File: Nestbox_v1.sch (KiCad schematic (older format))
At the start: 27 parts, among them P1 RX/TX, P2 TST/RST, P3 VDD/GND, Q1 SFH 3605, SW1 SMD-BUTTON_2P-3.0X2.5X1.2+0.4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, U1 MSP430FR5969, Y1 Crystal

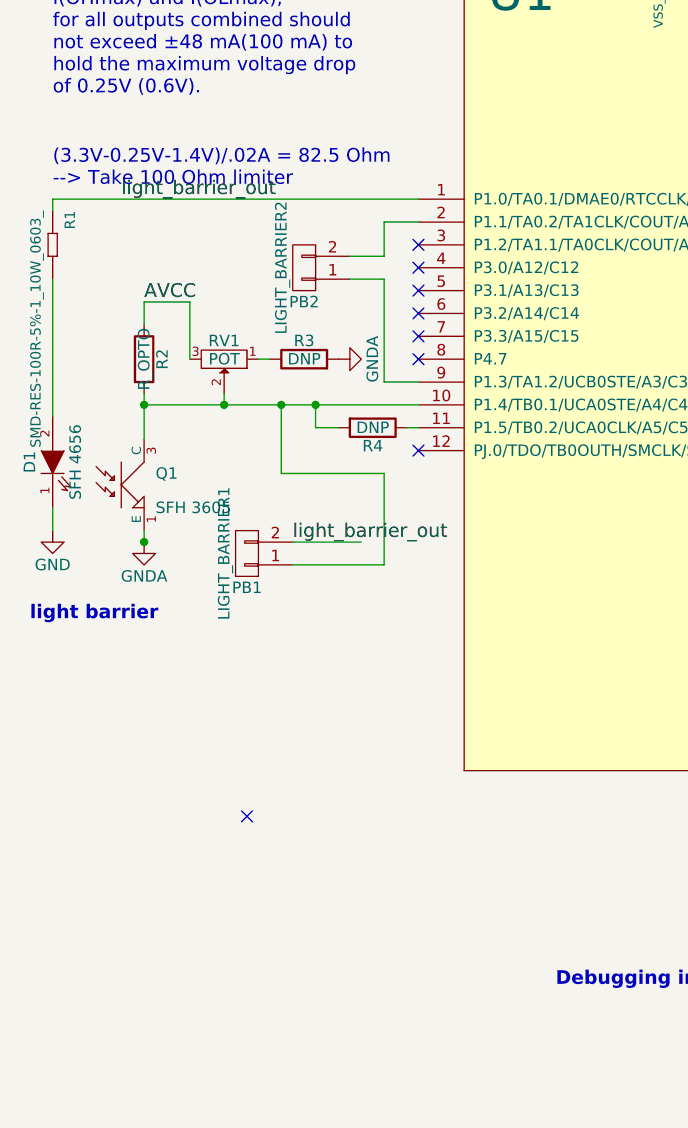
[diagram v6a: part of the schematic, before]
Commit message: added second phototransistor. started routing power and analog traces
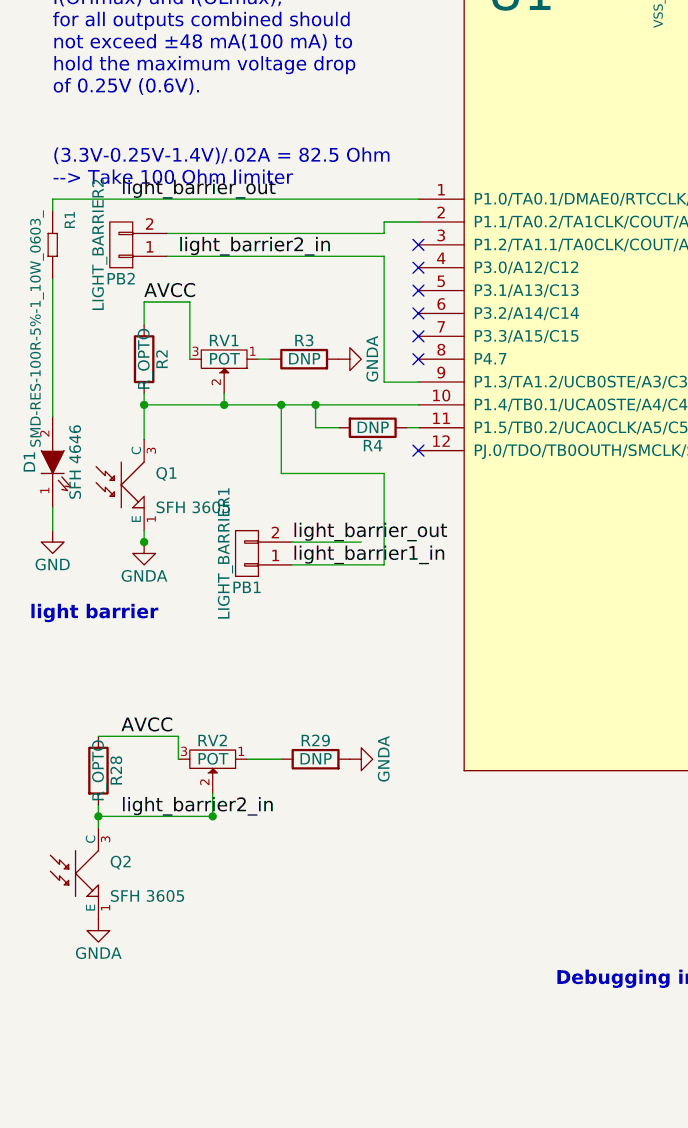
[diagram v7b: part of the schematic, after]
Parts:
- added Q2: SFH 3605, Octanis3:MIDLED_phototransistor, symbol OPTO_NPN
- added R28: R_OPTO, Resistors_SMD:R_0603, symbol R
- added R29: DNP, Resistors_SMD:R_0603, symbol R
- added RV2: POT, pot:3223G, symbol POT-RESCUE-Nestbox_v1
- D1: value SFH 4656 -> SFH 4646
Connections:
- net AVCC: now also R28.1, RV2.3
- net GND: now also Q2.1 (E), R29.2
- net light_barrier1_in: now reaches PB1.1 (P1), Q1.3 (C), R2.2, R4.2, RV1.2, U1.10 (P1.4/TB0.1/UCA0STE/A4/C4)
- net light_barrier2_in: now reaches PB2.1 (P1), U1.9 (P1.3/TA1.2/UCB0STE/A3/C3)
- net light_barrier2_in: now also Q2.3 (C), R28.2, RV2.2
- new net: R29.1, RV2.1
- no-connect marks 20 -> 19
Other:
- moved on the sheet: PB2
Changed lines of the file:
@@
 P 650 4250
 F 0 "D1" H 650 4350 50  0000 C CNN
-F 1 "SFH 4656" H 650 4150 50  0000 C CNN
+F 1 "SFH 4646" H 650 4150 50  0000 C CNN
 F 2 "Octanis3:MIDLED" H 650 4250 50  0001 C CNN
 F 3 "" H 650 4250 50  0000 C CNN
@@
 Wire Wire Line
 	3150 1750 3150 1800
-NoConn ~ 1500 5800
 $Comp
 L CERAMIC-10UF-25V-10%-X5R_0805_ C4
@@
 L CONN_01X02 PB2
 U 1 1 58BA717E
-P 1750 3400
-F 0 "PB2" H 1750 3550 50  0000 C CNN
-F 1 "LIGHT_BARRIER2" V 1850 3400 50  0000 C CNN
-F 2 "Socket_Strips:Socket_Strip_Straight_1x02" H 1750 3400 50  0001 C CNN
-F 3 "" H 1750 3400 50  0000 C CNN
-	1    1750 3400
+P 950 3300
+F 0 "PB2" H 950 3450 50  0000 C CNN
+F 1 "LIGHT_BARRIER2" V 1050 3300 50  0000 C CNN
+F 2 "Socket_Strips:Socket_Strip_Straight_1x02" H 950 3300 50  0001 C CNN
+F 3 "" H 950 3300 50  0000 C CNN
+	1    950  3300
 	-1   0    0    1
 $EndComp
@@
 	2250 3900 2100 3900
 Wire Wire Line
-	2100 3900 2100 3450
-Wire Wire Line
-	2100 3450 1950 3450
+	2100 3900 2100 3350
+Wire Wire Line
+	2100 3350 1150 3350
 Wire Wire Line
 	2250 3200 2100 3200
 Wire Wire Line
-	2100 3200 2100 3350
-Wire Wire Line
-	2100 3350 1950 3350
+	2100 3200 2100 3250
+Wire Wire Line
+	2100 3250 1150 3250
 Wire Wire Line
 	4800 6000 5600 6000
@@
 Text Label 1700 4600 0    60   ~ 0
 light_barrier_out
+$Comp
+L GNDA #PWR032
+U 1 1 58BD1039
+P 850 6250
+F 0 "#PWR032" H 850 6000 50  0001 C CNN
+F 1 "GNDA" H 850 6100 50  0000 C CNN
+F 2 "" H 850 6250 50  0000 C CNN
+F 3 "" H 850 6250 50  0000 C CNN
+	1    850  6250
+	1    0    0    -1
+$EndComp
+$Comp
+L OPTO_NPN Q2
+U 1 1 58BD10E6
+P 750 6050
+F 0 "Q2" H 900 6100 50  0000 L CNN
+F 1 "SFH 3605" H 900 5950 50  0000 L CNN
+F 2 "Octanis3:MIDLED_phototransistor" H 750 6050 50  0001 C CNN
+F 3 "" H 750 6050 50  0000 C CNN
+	1    750  6050
+	1    0    0    -1
+$EndComp
+$Comp
+L R R28
+U 1 1 58BD118C
+P 850 5600
+F 0 "R28" V 930 5600 50  0000 C CNN
+F 1 "R_OPTO" V 850 5600 50  0000 C CNN
+F 2 "Resistors_SMD:R_0603" V 780 5600 50  0001 C CNN
+F 3 "" H 850 5600 50  0000 C CNN
+	1    850  5600
+	1    0    0    -1
+$EndComp
+$Comp
+L POT-RESCUE-Nestbox_v1 RV2
+U 1 1 58BD120A
+P 1350 5550
+F 0 "RV2" H 1350 5470 50  0000 C CNN
+F 1 "POT" H 1350 5550 50  0000 C CNN
+F 2 "pot:3223G" H 1350 5550 50  0001 C CNN
+F 3 "" H 1350 5550 50  0000 C CNN
+	1    1350 5550
+	-1   0    0    1
+$EndComp
+$Comp
+L R R29
+U 1 1 58BD1294
+P 1800 5550
+F 0 "R29" V 1880 5550 50  0000 C CNN
+F 1 "DNP" V 1800 5550 50  0000 C CNN
+F 2 "Resistors_SMD:R_0603" V 1730 5550 50  0001 C CNN
+F 3 "" H 1800 5550 50  0000 C CNN
+	1    1800 5550
+	0    -1   -1   0
+$EndComp
+Wire Wire Line
+	850  5450 1200 5450
+Wire Wire Line
+	1200 5450 1200 5550
+Wire Wire Line
+	1500 5550 1650 5550
+$Comp
+L GNDA #PWR033
+U 1 1 58BD155D
+P 1950 5550
+F 0 "#PWR033" H 1950 5300 50  0001 C CNN
+F 1 "GNDA" H 1950 5400 50  0000 C CNN
+F 2 "" H 1950 5550 50  0000 C CNN
+F 3 "" H 1950 5550 50  0000 C CNN
+	1    1950 5550
+	0    -1   -1   0
+$EndComp
+Text Label 950  5450 0    60   ~ 0
+AVCC
+Text Label 1700 4700 0    60   ~ 0
+light_barrier1_in
+Text Label 950  5800 0    60   ~ 0
+light_barrier2_in
+Text Label 1200 3350 0    60   ~ 0
+light_barrier2_in
+Wire Wire Line
+	1350 5800 1350 5700
+Wire Wire Line
+	850  5750 850  5850
+Wire Wire Line
+	850  5800 1350 5800
+Connection ~ 1350 5800
+Connection ~ 850  5800
 $EndSCHEMATC

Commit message: added schematic changes
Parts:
- added C29: CERAMIC-100NF-50V-10%-X7R_0603_, SeeedOPL-Capacitor-2016:C0603, symbol CERAMIC-100NF-50V-10%-X7R_0603_
- added R30: SMD-RES-10K-1%-1_10W_0603_, SeeedOPL-Resistor-2016:R0603, symbol SMD-RES-10K-1%-1_10W_0603_
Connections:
- net GND: now also C29.2
- net at R7.1, SW1.2, U1.18 (P4.2/A10): now also R30.1
- new net: C29.1, R30.2
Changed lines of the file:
@@
 $EndComp
 $Comp
-L GND #PWR01
+L GND #PWR25
 U 1 1 586416A7
 P 6850 3100
-F 0 "#PWR01" H 6850 2850 50  0001 C CNN
+F 0 "#PWR25" H 6850 2850 50  0001 C CNN
 F 1 "GND" H 6850 2950 50  0000 C CNN
 F 2 "" H 6850 3100 50  0000 C CNN
@@
 $EndComp
 $Comp
-L +3.3V #PWR02
+L +3.3V #PWR17
 U 1 1 586418DC
 P 5000 1450
-F 0 "#PWR02" H 5000 1300 50  0001 C CNN
+F 0 "#PWR17" H 5000 1300 50  0001 C CNN
 F 1 "+3.3V" H 5000 1590 50  0000 C CNN
 F 2 "" H 5000 1450 50  0000 C CNN
@@
 $EndComp
 $Comp
-L GND #PWR03
+L GND #PWR7
 U 1 1 58641ADD
 P 3200 1600
-F 0 "#PWR03" H 3200 1350 50  0001 C CNN
+F 0 "#PWR7" H 3200 1350 50  0001 C CNN
 F 1 "GND" H 3200 1450 50  0000 C CNN
 F 2 "" H 3200 1600 50  0000 C CNN
@@
 $EndComp
 $Comp
-L +3.3V #PWR04
+L +3.3V #PWR8
 U 1 1 58641B00
 P 3550 1050
-F 0 "#PWR04" H 3550 900 50  0001 C CNN
+F 0 "#PWR8" H 3550 900 50  0001 C CNN
 F 1 "+3.3V" H 3550 1190 50  0000 C CNN
 F 2 "" H 3550 1050 50  0000 C CNN
@@
 $EndComp
 $Comp
-L GND #PWR05
+L GND #PWR18
 U 1 1 58652F3A
 P 5350 1800
-F 0 "#PWR05" H 5350 1550 50  0001 C CNN
+F 0 "#PWR18" H 5350 1550 50  0001 C CNN
 F 1 "GND" H 5350 1650 50  0000 C CNN
 F 2 "" H 5350 1800 50  0000 C CNN
@@
 $EndComp
 $Comp
-L GND #PWR06
+L GND #PWR11
 U 1 1 5865358A
 P 4100 950
-F 0 "#PWR06" H 4100 700 50  0001 C CNN
+F 0 "#PWR11" H 4100 700 50  0001 C CNN
 F 1 "GND" H 4100 800 50  0000 C CNN
 F 2 "" H 4100 950 50  0000 C CNN
@@
 $EndComp
 $Comp
-L GND #PWR07
+L GND #PWR27
 U 1 1 5865405F
 P 7500 1000
-F 0 "#PWR07" H 7500 750 50  0001 C CNN
+F 0 "#PWR27" H 7500 750 50  0001 C CNN
 F 1 "GND" H 7500 850 50  0000 C CNN
 F 2 "" H 7500 1000 50  0000 C CNN
@@
 $EndComp
 $Comp
-L +3.3V #PWR08
+L +3.3V #PWR29
 U 1 1 58654094
 P 7750 1000
-F 0 "#PWR08" H 7750 850 50  0001 C CNN
+F 0 "#PWR29" H 7750 850 50  0001 C CNN
 F 1 "+3.3V" H 7750 1140 50  0000 C CNN
 F 2 "" H 7750 1000 50  0000 C CNN
@@
 $EndComp
 $Comp
-L PWR_FLAG #FLG09
+L PWR_FLAG #FLG3
 U 1 1 58654135
 P 7750 1000
-F 0 "#FLG09" H 7750 1095 50  0001 C CNN
+F 0 "#FLG3" H 7750 1095 50  0001 C CNN
 F 1 "PWR_FLAG" H 7750 1180 50  0000 C CNN
 F 2 "" H 7750 1000 50  0000 C CNN
@@
 $EndComp
 $Comp
-L GND #PWR010
+L GND #PWR1
 U 1 1 587A72FE
 P 650 4550
-F 0 "#PWR010" H 650 4300 50  0001 C CNN
+F 0 "#PWR1" H 650 4300 50  0001 C CNN
 F 1 "GND" H 650 4400 50  0000 C CNN
 F 2 "" H 650 4550 50  0000 C CNN
@@
 $EndComp
 $Comp
-L GNDA #PWR011
+L GNDA #PWR4
 U 1 1 587B665F
 P 1900 3800
-F 0 "#PWR011" H 1900 3550 50  0001 C CNN
+F 0 "#PWR4" H 1900 3550 50  0001 C CNN
 F 1 "GNDA" H 1900 3650 50  0000 C CNN
 F 2 "" H 1900 3800 50  0000 C CNN
@@
 $EndComp
 $Comp
-L GNDA #PWR012
+L GNDA #PWR3
 U 1 1 587B6770
 P 1050 4600
-F 0 "#PWR012" H 1050 4350 50  0001 C CNN
+F 0 "#PWR3" H 1050 4350 50  0001 C CNN
 F 1 "GNDA" H 1050 4450 50  0000 C CNN
 F 2 "" H 1050 4600 50  0000 C CNN
@@
 $EndComp
 $Comp
-L GNDA #PWR013
+L GNDA #PWR9
 U 1 1 587B6902
 P 4000 1750
-F 0 "#PWR013" H 4000 1500 50  0001 C CNN
+F 0 "#PWR9" H 4000 1500 50  0001 C CNN
 F 1 "GNDA" H 4000 1600 50  0000 C CNN
 F 2 "" H 4000 1750 50  0000 C CNN
@@
 $EndComp
 $Comp
-L GNDA #PWR014
+L GNDA #PWR12
 U 1 1 587B69F1
 P 4300 1750
-F 0 "#PWR014" H 4300 1500 50  0001 C CNN
+F 0 "#PWR12" H 4300 1500 50  0001 C CNN
 F 1 "GNDA" H 4300 1600 50  0000 C CNN
 F 2 "" H 4300 1750 50  0000 C CNN
@@
 $EndComp
 $Comp
-L GNDA #PWR015
+L GNDA #PWR14
 U 1 1 587B6A2F
 P 4600 1750
-F 0 "#PWR015" H 4600 1500 50  0001 C CNN
+F 0 "#PWR14" H 4600 1500 50  0001 C CNN
 F 1 "GNDA" H 4600 1600 50  0000 C CNN
 F 2 "" H 4600 1750 50  0000 C CNN
@@
 $EndComp
 $Comp
-L GND #PWR016
+L GND #PWR15
 U 1 1 587B96DD
 P 4650 6400
-F 0 "#PWR016" H 4650 6150 50  0001 C CNN
+F 0 "#PWR15" H 4650 6150 50  0001 C CNN
 F 1 "GND" H 4650 6250 50  0000 C CNN
 F 2 "" H 4650 6400 50  0000 C CNN
@@
 $EndComp
 $Comp
-L +3.3V #PWR017
+L +3.3V #PWR16
 U 1 1 587B9736
 P 4650 7600
-F 0 "#PWR017" H 4650 7450 50  0001 C CNN
+F 0 "#PWR16" H 4650 7450 50  0001 C CNN
 F 1 "+3.3V" H 4650 7740 50  0000 C CNN
 F 2 "" H 4650 7600 50  0000 C CNN
@@
 $EndComp
 $Comp
-L GND #PWR018
+L GND #PWR13
 U 1 1 587B97E4
 P 4300 6850
-F 0 "#PWR018" H 4300 6600 50  0001 C CNN
+F 0 "#PWR13" H 4300 6600 50  0001 C CNN
 F 1 "GND" H 4300 6700 50  0000 C CNN
 F 2 "" H 4300 6850 50  0000 C CNN
@@
 $EndComp
 $Comp
-L GND #PWR019
+L GND #PWR10
 U 1 1 587B9834
 P 4000 6850
-F 0 "#PWR019" H 4000 6600 50  0001 C CNN
+F 0 "#PWR10" H 4000 6600 50  0001 C CNN
 F 1 "GND" H 4000 6700 50  0000 C CNN
 F 2 "" H 4000 6850 50  0000 C CNN
@@
 $EndComp
 $Comp
-L +3.3V #PWR020
+L +3.3V #PWR22
 U 1 1 587BBBBA
 P 6200 6300
-F 0 "#PWR020" H 6200 6150 50  0001 C CNN
+F 0 "#PWR22" H 6200 6150 50  0001 C CNN
 F 1 "+3.3V" H 6200 6440 50  0000 C CNN
 F 2 "" H 6200 6300 50  0000 C CNN
@@
 $EndComp
 $Comp
-L GND #PWR021
+L GND #PWR21
 U 1 1 587BBC10
 P 6100 6300
-F 0 "#PWR021" H 6100 6050 50  0001 C CNN
+F 0 "#PWR21" H 6100 6050 50  0001 C CNN
 F 1 "GND" H 6100 6150 50  0000 C CNN
 F 2 "" H 6100 6300 50  0000 C CNN
@@
 LORA_RX
 $Comp
-L +BATT #PWR022
+L +BATT #PWR30
 U 1 1 587BD5F5
 P 8000 1000
-F 0 "#PWR022" H 8000 850 50  0001 C CNN
+F 0 "#PWR30" H 8000 850 50  0001 C CNN
 F 1 "+BATT" H 8000 1140 50  0000 C CNN
 F 2 "" H 8000 1000 50  0000 C CNN
@@
 $EndComp
 $Comp
-L PWR_FLAG #FLG023
+L PWR_FLAG #FLG4
 U 1 1 587BD64F
 P 8000 1000
-F 0 "#FLG023" H 8000 1095 50  0001 C CNN
+F 0 "#FLG4" H 8000 1095 50  0001 C CNN
 F 1 "PWR_FLAG" H 8000 1180 50  0000 C CNN
 F 2 "" H 8000 1000 50  0000 C CNN
@@
 NoConn ~ 4900 1800
 $Comp
-L PWR_FLAG #FLG024
+L PWR_FLAG #FLG1
 U 1 1 587C02BB
 P 7500 900
-F 0 "#FLG024" H 7500 995 50  0001 C CNN
+F 0 "#FLG1" H 7500 995 50  0001 C CNN
 F 1 "PWR_FLAG" H 7500 1080 50  0000 C CNN
 F 2 "" H 7500 900 50  0000 C CNN
@@
 $EndComp
 $Comp
-L GND #PWR025
+L GND #PWR26
 U 1 1 587C0E96
 P 6950 1050
-F 0 "#PWR025" H 6950 800 50  0001 C CNN
+F 0 "#PWR26" H 6950 800 50  0001 C CNN
 F 1 "GND" H 6950 900 50  0000 C CNN
 F 2 "" H 6950 1050 50  0000 C CNN
@@
 $EndComp
 $Comp
-L GNDA #PWR026
+L GNDA #PWR24
 U 1 1 587C0F20
 P 6750 1050
-F 0 "#PWR026" H 6750 800 50  0001 C CNN
+F 0 "#PWR24" H 6750 800 50  0001 C CNN
 F 1 "GNDA" H 6750 900 50  0000 C CNN
 F 2 "" H 6750 1050 50  0000 C CNN
@@
 $EndComp
 $Comp
-L GNDPWR #PWR027
+L GNDPWR #PWR23
 U 1 1 587C0FCC
 P 6550 1100
-F 0 "#PWR027" H 6550 900 50  0001 C CNN
+F 0 "#PWR23" H 6550 900 50  0001 C CNN
 F 1 "GNDPWR" H 6550 970 50  0000 C CNN
 F 2 "" H 6550 1050 50  0000 C CNN
@@
 	4650 7100 4650 7200
 Wire Wire Line
-	4650 7150 4550 7150
+	4550 7150 4800 7150
 Wire Wire Line
 	4550 7150 4550 6100
@@
 	7300 4000 6850 4000
 $Comp
-L VDDA #PWR028
+L VDDA #PWR28
 U 1 1 587C8C74
 P 7500 1500
-F 0 "#PWR028" H 7500 1350 50  0001 C CNN
+F 0 "#PWR28" H 7500 1350 50  0001 C CNN
 F 1 "VDDA" H 7500 1650 50  0000 C CNN
 F 2 "" H 7500 1500 50  0000 C CNN
@@
 $EndComp
 $Comp
-L PWR_FLAG #FLG029
+L PWR_FLAG #FLG2
 U 1 1 587C8CD0
 P 7500 1500
-F 0 "#FLG029" H 7500 1595 50  0001 C CNN
+F 0 "#FLG2" H 7500 1595 50  0001 C CNN
 F 1 "PWR_FLAG" H 7500 1680 50  0000 C CNN
 F 2 "" H 7500 1500 50  0000 C CNN
@@
 	4000 6550 4000 6500
 $Comp
-L GND #PWR030
+L GND #PWR6
 U 1 1 587D2523
 P 3150 1800
-F 0 "#PWR030" H 3150 1550 50  0001 C CNN
+F 0 "#PWR6" H 3150 1550 50  0001 C CNN
 F 1 "GND" H 3150 1650 50  0000 C CNN
 F 2 "" H 3150 1800 50  0000 C CNN
@@
 	5600 6000 5600 6250
 $Comp
-L +3.3V #PWR031
+L +3.3V #PWR20
 U 1 1 58BC4BB7
 P 6100 5950
-F 0 "#PWR031" H 6100 5800 50  0001 C CNN
+F 0 "#PWR20" H 6100 5800 50  0001 C CNN
 F 1 "+3.3V" H 6100 6090 50  0000 C CNN
 F 2 "" H 6100 5950 50  0000 C CNN
@@
 light_barrier_out
 $Comp
-L GNDA #PWR032
+L GNDA #PWR2
 U 1 1 58BD1039
 P 850 6250
-F 0 "#PWR032" H 850 6000 50  0001 C CNN
+F 0 "#PWR2" H 850 6000 50  0001 C CNN
 F 1 "GNDA" H 850 6100 50  0000 C CNN
 F 2 "" H 850 6250 50  0000 C CNN
@@
 	1500 5550 1650 5550
 $Comp
-L GNDA #PWR033
+L GNDA #PWR5
 U 1 1 58BD155D
 P 1950 5550
-F 0 "#PWR033" H 1950 5300 50  0001 C CNN
+F 0 "#PWR5" H 1950 5300 50  0001 C CNN
 F 1 "GNDA" H 1950 5400 50  0000 C CNN
 F 2 "" H 1950 5550 50  0000 C CNN
@@
 Connection ~ 1350 5800
 Connection ~ 850  5800
+$Comp
+L SMD-RES-10K-1%-1_10W_0603_ R30
+U 1 1 58BF0F5A
+P 4950 7150
+F 0 "R30" H 4800 7200 45  0000 L BNN
+F 1 "SMD-RES-10K-1%-1_10W_0603_" H 4800 7050 45  0000 L BNN
+F 2 "SeeedOPL-Resistor-2016:R0603" H 4950 7150 40  0001 C CNN
+F 3 "" H 4950 7150 40  0001 C CNN
+F 4 "RC0603FR-0710KL" H 4980 7300 20  0001 C CNN "MPN"
+F 5 "301010299" H 4980 7300 20  0001 C CNN "SKU"
+	1    4950 7150
+	1    0    0    -1
+$EndComp
+$Comp
+L CERAMIC-100NF-50V-10%-X7R_0603_ C29
+U 1 1 58BF15A3
+P 5400 7050
+F 0 "C29" H 5250 7100 45  0000 L BNN
+F 1 "CERAMIC-100NF-50V-10%-X7R_0603_" H 5250 6950 45  0000 L BNN
+F 2 "SeeedOPL-Capacitor-2016:C0603" H 5400 7050 60  0001 C CNN
+F 3 "" H 5400 7050 60  0001 C CNN
+F 4 "CC0603KRX7R9BB104" H 5430 7200 20  0001 C CNN "MPN"
+F 5 "302010138" H 5430 7200 20  0001 C CNN "SKU"
+	1    5400 7050
+	1    0    0    -1
+$EndComp
+Wire Wire Line
+	5100 7150 5100 7050
+Wire Wire Line
+	5100 7050 5250 7050
+$Comp
+L GND #PWR19
+U 1 1 58BF19D6
+P 5650 7050
+F 0 "#PWR19" H 5650 6800 50  0001 C CNN
+F 1 "GND" H 5650 6900 50  0000 C CNN
+F 2 "" H 5650 7050 50  0000 C CNN
+F 3 "" H 5650 7050 50  0000 C CNN
+	1    5650 7050
+	0    -1   -1   0
+$EndComp
+Wire Wire Line
+	5550 7050 5650 7050
 $EndSCHEMATC
